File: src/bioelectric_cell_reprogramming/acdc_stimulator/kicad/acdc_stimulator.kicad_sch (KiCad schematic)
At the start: 67 parts, among them IC1 AD9833BRM-REEL7, IC2 AD5122BCPZ10-RL7, J1 Screw_Terminal_01x02, J2 Conn_ARM_SWD_TagConnect_TC203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, J3 USB_C_Receptacle_USB2.0_14P, J4 S4B-PH-SM4-TB, J5 IPL1-102-01-L-S-K, J6 Screw_Terminal_01x02, J7 IPL1-102-01-L-S-K, Q1 BSZ096N10LS5ATMA1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

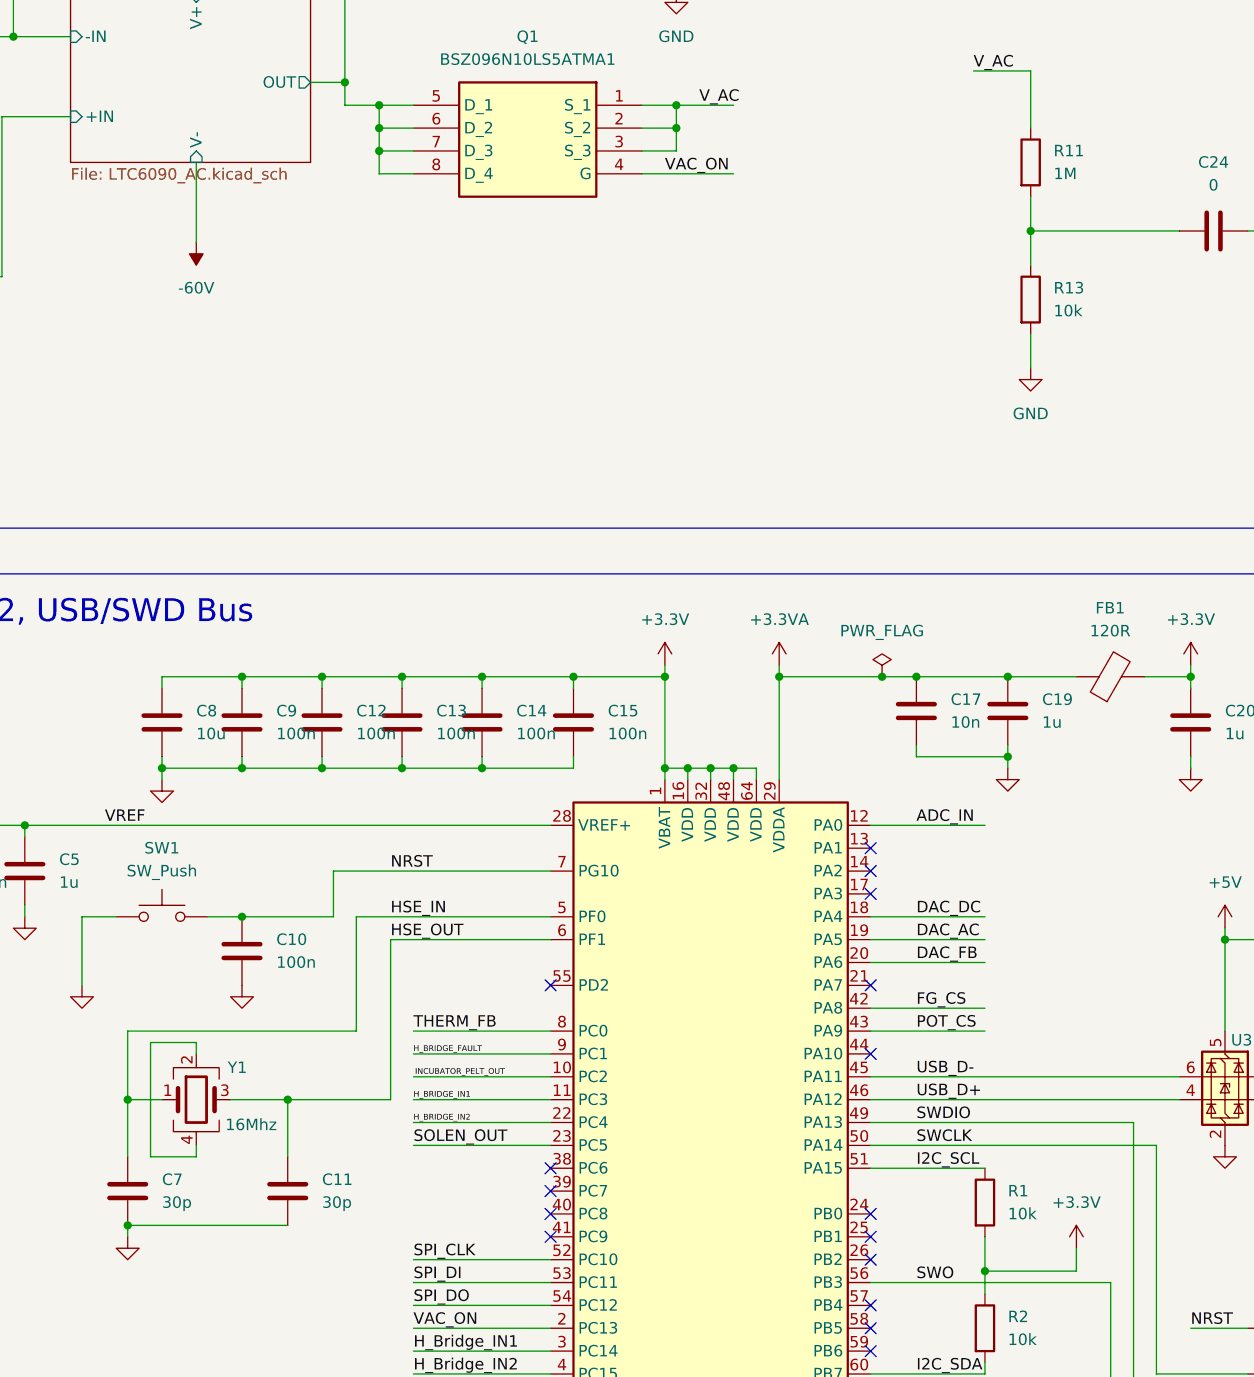
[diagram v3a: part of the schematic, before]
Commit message: ci: BOM done
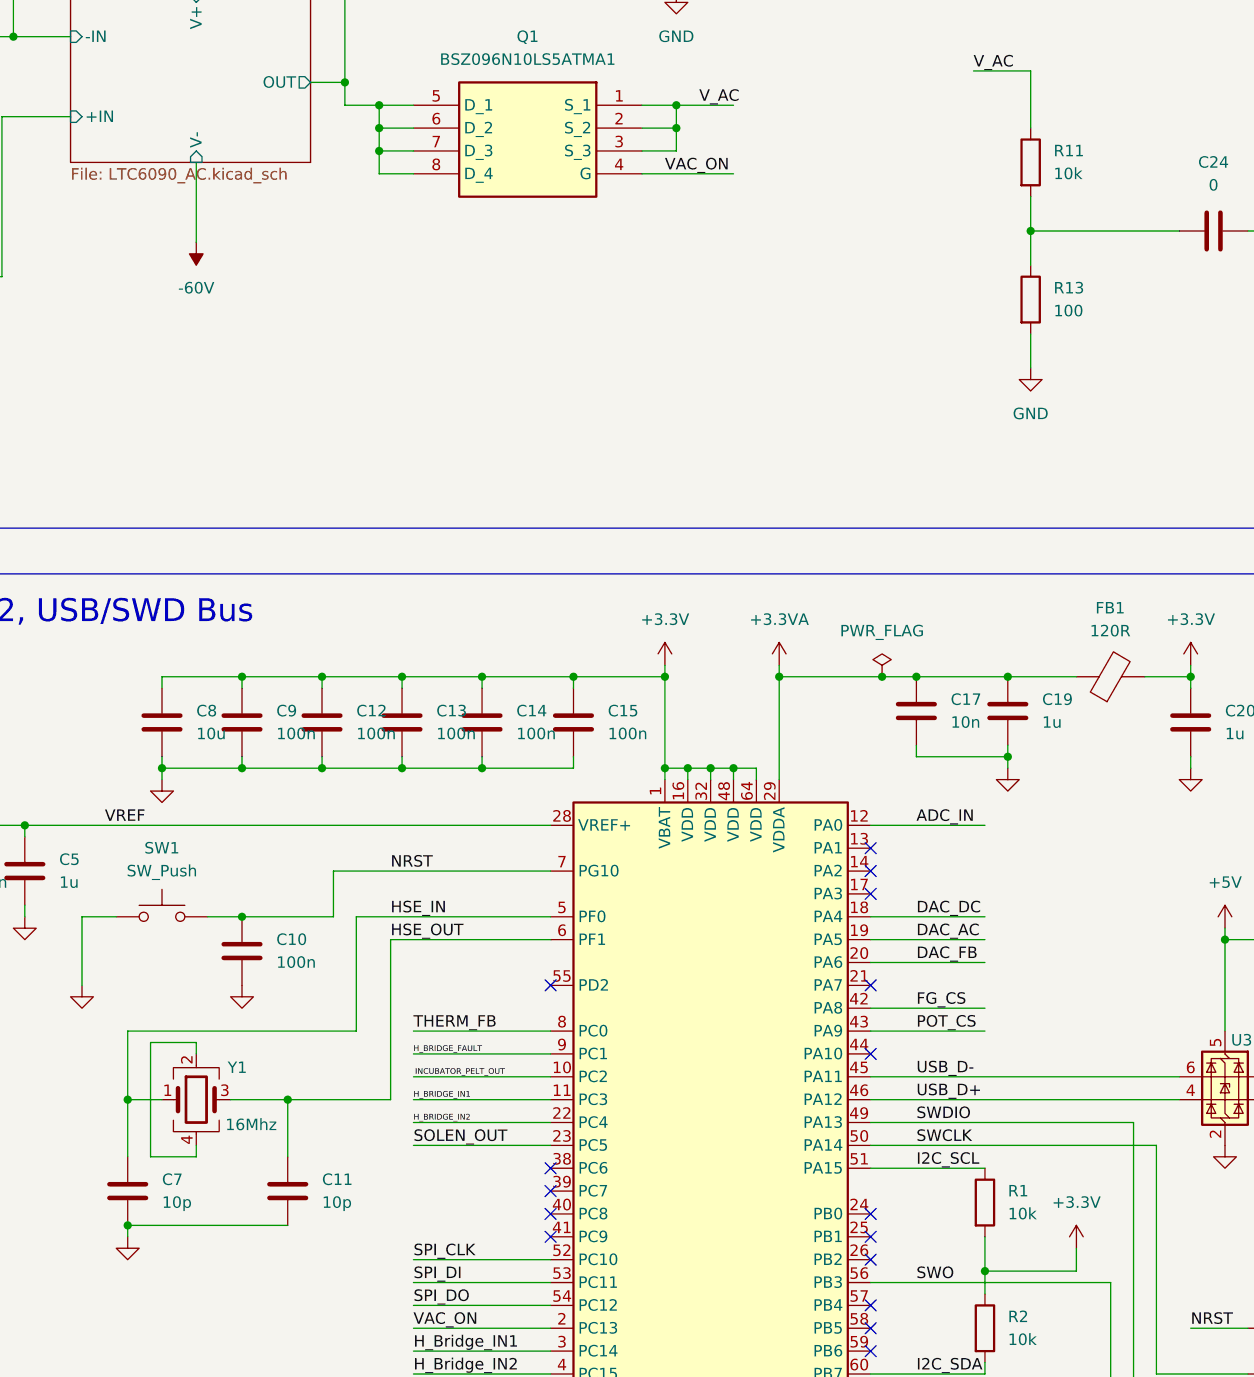
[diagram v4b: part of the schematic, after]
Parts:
- C11, C7: value 30p -> 10p
- D1: Distributor Link (none) -> https://jlcpcb.com/partdetail/EverlightElec-16_213SDRC_S530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; Manufacturer (none) -> Everlight Elec; Manufacturer Part Number (none) -> 16-213SDRC/S530-A3/TR8
- F1: Distributor Link (none) -> https://jlcpcb.com/partdetail/21501-SMD0603P050TF/C20789; Manufacturer (none) -> RUILON(Shenzhen Ruilongyuan Elec); Manufacturer Part Number (none) -> SMD0603P050TF
- FB1: Distributor Link (none) -> https://jlcpcb.com/partdetail/MurataElectronics-BLM18PG121S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; Manufacturer (none) -> Murata Electronics; Manufacturer Part Number (none) -> BLM18PG121SN1D
- IC1: Distributor Link (none) -> https://jlcpcb.com/partdetail/AnalogDevices-AD9833BRMZREEL7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; Manufacturer (none) -> Analog Devices; Manufacturer Part Number (none) -> AD9833BRMZ-REEL7
- J3: footprint Connector_USB:USB_C_Receptacle_GCT_USB4105-xx-A_16P_TopMnt_Horizontal -> Connector_USB:USB_C_Receptacle_XKB_U262-16XN-4BVC11; Distributor Link (none) -> https://jlcpcb.com/partdetail/XkbConnection-U262_161N4BVC11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; Manufacturer (none) -> XKB Connection; Manufacturer Part Number (none) -> U262-161N-4BVC11
- J4: Distributor Link (none) -> https://jlcpcb.com/partdetail/Jst-S4B_PH_SM4_TB_LF_SN/C2651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; Manufacturer (none) -> JST; Manufacturer Part Number (none) -> S4B-PH-SM4-TB(LF)(SN)
- Q2: Distributor Link (none) -> https://jlcpcb.com/partdetail/Onsemi-NDT3055L/C274612; Manufacturer (none) -> onsemi; Manufacturer Part Number (none) -> NDT3055L
- R10: Distributor Link (none) -> https://jlcpcb.com/partdetail/18087-0805W8F1804T5E/C17399; Manufacturer (none) -> UNI-ROYAL(Uniroyal Elec); Manufacturer Part Number (none) -> 0805W8F1804T5E
- R11: value 1M -> 10k; footprint Resistor_SMD:R_0603_1608Metric -> Resistor_SMD:R_0805_2012Metric; Distributor Link (none) -> https://jlcpcb.com/partdetail/Ever_OhmsTech-QR0805J10K0P05Z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; Manufacturer (none) -> Ever Ohms Tech; Manufacturer Part Number (none) -> QR0805J10K0P05Z
- R13: value 10k -> 100; footprint Resistor_SMD:R_0402_1005Metric -> Resistor_SMD:R_0805_2012Metric; Distributor Link https://jlcpcb.com/partdetail/259901-NQ02WGJ0103TCE/C270371 -> https://jlcpcb.com/partdetail/18096-0805W8F1000T5E/C17408; Manufacturer Part Number NQ02WGJ0103TCE -> 0805W8F1000T5E
- R14: Distributor Link (none) -> https://jlcpcb.com/partdetail/Yageo-RT0603BRD07172KL/C861162; Manufacturer (none) -> YAGEO; Manufacturer Part Number (none) -> RT0603BRD07172KL
- R4: Distributor Link (none) -> https://jlcpcb.com/partdetail/12256-0402WGF1001TCE/C11702; Manufacturer (none) -> UNI-ROYAL(Uniroyal Elec); Manufacturer Part Number (none) -> 0402WGF1001TCE
- R9: Distributor Link (none) -> https://jlcpcb.com/partdetail/18202-0805W8F1004T5E/C17514; Manufacturer (none) -> UNI-ROYAL(Uniroyal Elec); Manufacturer Part Number (none) -> 0805W8F1004T5E
- SW2: Distributor Link (none) -> https://jlcpcb.com/partdetail/ck-PCM12SMTR/C221841; Manufacturer (none) -> C&K; Manufacturer Part Number (none) -> PCM12SMTR
- U1: Distributor Link (none) -> https://jlcpcb.com/partdetail/Stmicroelectronics-STM32G473R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; Manufacturer (none) -> STMicroelectronics; Manufacturer Part Number (none) -> STM32G473RCT6
- U2: Distributor Link (none) -> https://jlcpcb.com/partdetail/Advanced_MonolithicSystems-AM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; Manufacturer (none) -> Advanced Monolithic Systems; Manufacturer Part Number (none) -> AMS1117-3.3
- U3: Distributor Link (none) -> https://jlcpcb.com/partdetail/Stmicroelectronics-USBLC62SC6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; Manufacturer (none) -> STMicroelectronics; Manufacturer Part Number (none) -> USBLC6-2SC6
- Y1: Distributor Link (none) -> https://jlcpcb.com/partdetail/TxcCorp-7M16000024/C90905; Manufacturer (none) -> TXC Corp; Manufacturer Part Number (none) -> 7M16000024
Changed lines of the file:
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@@
 			)
 		)
-		(property "Footprint" "Connector_USB:USB_C_Receptacle_GCT_USB4105-xx-A_16P_TopMnt_Horizontal"
+		(property "Footprint" "Connector_USB:USB_C_Receptacle_XKB_U262-16XN-4BVC11"
 			(at 204.47 204.47 0)
 			(effects
@@
 			)
 		)
-		(property "Distributor Link" ""
+		(property "Distributor Link" "https://jlcpcb.com/partdetail/XkbConnection-U262_161N4BVC11/C319148"
 			(at 208.28 204.47 0)
 			(effects
@@
 			)
 		)
-		(property "Manufacturer" ""
+		(property "Manufacturer" "XKB Connection"
 			(at 208.28 204.47 0)
 			(effects
@@
 			)
 		)
-		(property "Manufacturer Part Number" ""
+		(property "Manufacturer Part Number" "U262-161N-4BVC11"
 			(at 208.28 204.47 0)
 			(effects
@@
 			)
 		)
-		(property "Distributor Link" ""
+		(property "Distributor Link" "https://jlcpcb.com/partdetail/18087-0805W8F1804T5E/C17399"
 			(at 60.96 72.39 0)
 			(effects
@@
 			)
 		)
-		(property "Manufacturer" ""
+		(property "Manufacturer" "UNI-ROYAL(Uniroyal Elec)"
 			(at 60.96 72.39 0)
 			(effects
@@
 			)
 		)
-		(property "Manufacturer Part Number" ""
+		(property "Manufacturer Part Number" "0805W8F1804T5E"
 			(at 60.96 72.39 0)
 			(effects
@@
 			)
 		)
-		(property "Value" "30p"
+		(property "Value" "10p"
 			(at 49.53 218.4399 0)
 			(effects
@@
 			)
 		)
-		(property "Distributor Link" ""
+		(property "Distributor Link" "https://jlcpcb.com/partdetail/21501-SMD0603P050TF/C20789"
 			(at 179.07 189.23 0)
 			(effects
@@
 			)
 		)
-		(property "Manufacturer" ""
+		(property "Manufacturer" "RUILON(Shenzhen Ruilongyuan Elec)"
 			(at 179.07 189.23 0)
 			(effects
@@
 			)
 		)
-		(property "Manufacturer Part Number" ""
+		(property "Manufacturer Part Number" "SMD0603P050TF"
 			(at 179.07 189.23 0)
 			(effects
@@
 			)
 		)
-		(property "Distributor Link" ""
+		(property "Distributor Link" "https://jlcpcb.com/partdetail/Stmicroelectronics-STM32G473RCT6/C529361"
 			(at 110.49 219.71 0)
 			(effects
@@
 			)
 		)
-		(property "Manufacturer" ""
+		(property "Manufacturer" "STMicroelectronics"
 			(at 110.49 219.71 0)
 			(effects
@@
 			)
 		)
-		(property "Manufacturer Part Number" ""
+		(property "Manufacturer Part Number" "STM32G473RCT6"
 			(at 110.49 219.71 0)
 			(effects
@@
 			)
 		)
-		(property "Distributor Link" ""
+		(property "Distributor Link" "https://jlcpcb.com/partdetail/TxcCorp-7M16000024/C90905"
 			(at 53.34 207.01 0)
 			(effects
@@
 			)
 		)
-		(property "Manufacturer" ""
+		(property "Manufacturer" "TXC Corp"
 			(at 53.34 207.01 0)
 			(effects
@@
 			)
 		)
-		(property "Manufacturer Part Number" ""
+		(property "Manufacturer Part Number" "7M16000024"
 			(at 53.34 207.01 0)
 			(effects
@@
 			)
 		)
-		(property "Distributor Link" ""
+		(property "Distributor Link" "https://jlcpcb.com/partdetail/MurataElectronics-BLM18PG121SN1D/C14709"
 			(at 154.94 160.02 0)
 			(effects
@@
 			)
 		)
-		(property "Manufacturer" ""
+		(property "Manufacturer" "Murata Electronics"
 			(at 154.94 160.02 0)
 			(effects
@@
 			)
 		)
-		(property "Manufacturer Part Number" ""
+		(property "Manufacturer Part Number" "BLM18PG121SN1D"
 			(at 154.94 160.02 0)
 			(effects
@@
 			)
 		)
-		(property "Distributor Link" ""
+		(property "Distributor Link" "https://jlcpcb.com/partdetail/Advanced_MonolithicSystems-AMS1117_33/C6186"
 			(at 266.7 26.67 0)
 			(effects
@@
 			)
 		)
-		(property "Manufacturer" ""
+		(property "Manufacturer" " Advanced Monolithic Systems"
 			(at 266.7 26.67 0)
 			(effects
@@
 			)
 		)
-		(property "Manufacturer Part Number" ""
+		(property "Manufacturer Part Number" "AMS1117-3.3"
 			(at 266.7 26.67 0)
 			(effects
@@
 			)
 		)
-		(property "Distributor Link" ""
+		(property "Distributor Link" "https://jlcpcb.com/partdetail/EverlightElec-16_213SDRC_S530_A3TR8/C71911"
 			(at 287.02 26.67 0)
 			(effects
@@
 			)
 		)
-		(property "Manufacturer" ""
+		(property "Manufacturer" "Everlight Elec"
 			(at 287.02 26.67 0)
 			(effects
@@
 			)
 		)
-		(property "Manufacturer Part Number" ""
+		(property "Manufacturer Part Number" "16-213SDRC/S530-A3/TR8"
 			(at 287.02 26.67 0)
 			(effects
@@
 			)
 		)
-		(property "Distributor Link" ""
+		(property "Distributor Link" "https://jlcpcb.com/partdetail/Onsemi-NDT3055L/C274612"
 			(at 308.61 220.98 0)
 			(effects
@@
 			)
 		)
-		(property "Manufacturer" ""
+		(property "Manufacturer" "onsemi"
 			(at 308.61 220.98 0)
 			(effects
@@
 			)
 		)
-		(property "Manufacturer Part Number" ""
+		(property "Manufacturer Part Number" "NDT3055L"
 			(at 308.61 220.98 0)
 			(effects
@@
 			)
 		)
-		(property "Distributor Link" ""
+		(property "Distributor Link" "https://jlcpcb.com/partdetail/Yageo-RT0603BRD07172KL/C861162"
 			(at 254 90.17 0)
 			(effects
@@
 			)
 		)
-		(property "Manufacturer" ""
+		(property "Manufacturer" "YAGEO"
 			(at 254 90.17 0)
 			(effects
@@
 			)
 		)
-		(property "Manufacturer Part Number" ""
+		(property "Manufacturer Part Number" "RT0603BRD07172KL"
 			(at 254 90.17 0)
 			(effects
@@
 			)
 		)
-		(property "Value" "1M"
+		(property "Value" "10k"
 			(at 148.59 104.1399 0)
 			(effects
@@
 			)
 		)
-		(property "Footprint" "Resistor_SMD:R_0603_1608Metric"
+		(property "Footprint" "Resistor_SMD:R_0805_2012Metric"
 			(at 144.272 102.87 90)
 			(effects
@@
 			)
 		)
-		(property "Distributor Link" ""
+		(property "Distributor Link" "https://jlcpcb.com/partdetail/Ever_OhmsTech-QR0805J10K0P05Z/C149881"
 			(at 146.05 102.87 0)
 			(effects
@@
 			)
 		)
-		(property "Manufacturer" ""
+		(property "Manufacturer" "Ever Ohms Tech"
 			(at 146.05 102.87 0)
 			(effects
@@
 			)
 		)
-		(property "Manufacturer Part Number" ""
+		(property "Manufacturer Part Number" "QR0805J10K0P05Z"
 			(at 146.05 102.87 0)
 			(effects
@@
 			)
 		)
-		(property "Distributor Link" ""
+		(property "Distributor Link" "https://jlcpcb.com/partdetail/AnalogDevices-AD9833BRMZREEL7/C9652"
 			(at 40.64 40.64 0)
 			(effects
@@
 			)
 		)
-		(property "Manufacturer" ""
+		(property "Manufacturer" "Analog Devices"
 			(at 40.64 40.64 0)
 			(effects
@@
 			)
 		)
-		(property "Manufacturer Part Number" ""
+		(property "Manufacturer Part Number" "AD9833BRMZ-REEL7"
 			(at 40.64 40.64 0)
 			(effects
@@
 			)
 		)
-		(property "Value" "30p"
+		(property "Value" "10p"
 			(at 67.31 218.4399 0)
 			(effects
@@
 			)
 		)
-		(property "Distributor Link" ""
+		(property "Distributor Link" "https://jlcpcb.com/partdetail/Jst-S4B_PH_SM4_TB_LF_SN/C265102"
 			(at 275.59 168.91 0)
 			(effects
@@
 			)
 		)
-		(property "Manufacturer" ""
+		(property "Manufacturer" "JST"
 			(at 275.59 168.91 0)
 			(effects
@@
 			)
 		)
-		(property "Manufacturer Part Number" ""
+		(property "Manufacturer Part Number" "S4B-PH-SM4-TB(LF)(SN)"
 			(at 275.59 168.91 0)
 			(effects
@@
 			)
 		)
-		(property "Distributor Link" ""
+		(property "Distributor Link" "https://jlcpcb.com/partdetail/18202-0805W8F1004T5E/C17514"
 			(at 44.45 72.39 0)
 			(effects
@@
 			)
 		)
-		(property "Manufacturer" ""
+		(property "Manufacturer" "UNI-ROYAL(Uniroyal Elec)"
 			(at 44.45 72.39 0)
 			(effects
@@
 			)
 		)
-		(property "Manufacturer Part Number" ""
+		(property "Manufacturer Part Number" "0805W8F1004T5E"
 			(at 44.45 72.39 0)
 			(effects
@@
 			)
 		)
-		(property "Distributor Link" ""
+		(property "Distributor Link" "https://jlcpcb.com/partdetail/ck-PCM12SMTR/C221841"
 			(at 170.18 264.16 0)
 			(effects
@@
 			)
 		)
-		(property "Manufacturer" ""
+		(property "Manufacturer" "C&K"
 			(at 170.18 264.16 0)
 			(effects
@@
 			)
 		)
-		(property "Manufacturer Part Number" ""
+		(property "Manufacturer Part Number" "PCM12SMTR"
 			(at 170.18 264.16 0)
 			(effects
@@
 			)
 		)
-		(property "Distributor Link" ""
+		(property "Distributor Link" "https://jlcpcb.com/partdetail/12256-0402WGF1001TCE/C11702"
 			(at 299.72 33.02 0)
 			(effects
@@
 			)
 		)
-		(property "Manufacturer" ""
+		(property "Manufacturer" "UNI-ROYAL(Uniroyal Elec)"
 			(at 299.72 33.02 0)
 			(effects
@@
 			)
 		)
-		(property "Manufacturer Part Number" ""
+		(property "Manufacturer Part Number" "0402WGF1001TCE"
 			(at 299.72 33.02 0)
 			(effects
@@
 			)
 		)
-		(property "Value" "10k"
+		(property "Value" "100"
 			(at 148.59 119.3799 0)
 			(effects
@@
 			)
 		)
-		(property "Footprint" "Resistor_SMD:R_0402_1005Metric"
+		(property "Footprint" "Resistor_SMD:R_0805_2012Metric"
 			(at 144.272 118.11 90)
 			(effects
@@
 			)
 		)
-		(property "Distributor Link" "https://jlcpcb.com/partdetail/259901-NQ02WGJ0103TCE/C270371"
+		(property "Distributor Link" "https://jlcpcb.com/partdetail/18096-0805W8F1000T5E/C17408"
 			(at 146.05 118.11 0)
 			(effects
@@
 			)
 		)
-		(property "Manufacturer Part Number" "NQ02WGJ0103TCE"
+		(property "Manufacturer Part Number" "0805W8F1000T5E"
 			(at 146.05 118.11 0)
 			(effects
@@
 			)
 		)
-		(property "Distributor Link" ""
+		(property "Distributor Link" "https://jlcpcb.com/partdetail/Stmicroelectronics-USBLC62SC6/C7519"
 			(at 167.64 204.47 0)
 			(effects
@@
 			)
 		)
-		(property "Manufacturer" ""
+		(property "Manufacturer" "STMicroelectronics"
 			(at 167.64 204.47 0)
 			(effects
@@
 			)
 		)
-		(property "Manufacturer Part Number" ""
+		(property "Manufacturer Part Number" "USBLC6-2SC6"
 			(at 167.64 204.47 0)
 			(effects
